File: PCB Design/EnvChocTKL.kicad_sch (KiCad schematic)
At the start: 188 parts

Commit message: added mid-mount type-c port, swapped onboard MCU for pico and also couple more mount holes, various other adjustments i.e backplate n stuff
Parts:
- removed USB1: TYPE-C-31-M-12, HRO-TYPE-C31-M-12:HRO-TYPE-C-31-M-12, symbol Type-C:HRO-TYPE-C-31-M-12
- added H5, H6: MountingHole_Pad, MountingHole:MountingHole_2.5mm_Pad, symbol Mechanical:MountingHole_Pad
- added J1: Type-c-31-m-14, josh-connectors:USB_C_TYPE-C-31-M-14, symbol josh-connector:USB_C_U262-161N-4BVC11
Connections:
- net GND: now also H5.1, H6.1, J1.A1 (GND), J1.A12 (GND), J1.B1 (GND), J1.B12 (GND), J1.S1 (SHIELD)
- net USB_D+: now also J1.A6 (D+), J1.B6 (D+)
- net USB_D-: now also J1.A7 (D-), J1.B7 (D-)
- net VBUS: now also RPI1.40 (VBUS), J1.A4 (VBUS), J1.A9 (VBUS), J1.B4 (VBUS), J1.B9 (VBUS)
- net at R6.2: now also J1.B5 (CC2)
- net at R5.2: now also J1.A5 (CC1)
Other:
- moved on the sheet: D_0, D_1, D_10, D_11, D_12, D_13, D_14, D_15, D_16, D_17, D_18, D_19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

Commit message: generated updated gerber
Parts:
- R5, R6: value 5.1K 0402 -> 5.1K 0805; footprint Resistor_SMD:R_0402_1005Metric -> Resistor_SMD:R_0805_2012Metric
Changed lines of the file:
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@@
   (symbol (lib_id "Device:R_Small") (at 50.165 46.355 270) (unit 1)
     (in_bom yes) (on_board yes)
-    (property "Reference" "R6" (id 0) (at 50.165 43.815 90))
-    (property "Value" "5.1K 0402" (id 1) (at 50.165 46.355 90)
+    (property "Reference" "R6" (id 0) (at 50.165 48.26 90))
+    (property "Value" "5.1K 0805" (id 1) (at 50.165 46.355 90)
       (effects (font (size 0.508 0.508)))
     )
-    (property "Footprint" "Resistor_SMD:R_0402_1005Metric" (id 2) (at 50.165 46.355 0)
+    (property "Footprint" "Resistor_SMD:R_0805_2012Metric" (id 2) (at 50.165 46.355 0)
       (effects (font (size 1.27 1.27)) hide)
     )
@@
     (in_bom yes) (on_board yes)
     (property "Reference" "R5" (id 0) (at 50.165 41.275 90))
-    (property "Value" "5.1K 0402" (id 1) (at 50.165 43.815 90)
+    (property "Value" "5.1K 0805" (id 1) (at 50.165 43.815 90)
       (effects (font (size 0.508 0.508)))
     )
-    (property "Footprint" "Resistor_SMD:R_0402_1005Metric" (id 2) (at 50.165 43.815 0)
+    (property "Footprint" "Resistor_SMD:R_0805_2012Metric" (id 2) (at 50.165 43.815 0)
       (effects (font (size 1.27 1.27)) hide)
     )
@@
     )
     (path "/00000000-0000-0000-0000-00006093a5b0"
-      (reference "R5") (unit 1) (value "5.1K 0402") (footprint "Resistor_SMD:R_0402_1005Metric")
+      (reference "R5") (unit 1) (value "5.1K 0805") (footprint "Resistor_SMD:R_0805_2012Metric")
     )
     (path "/00000000-0000-0000-0000-0000609385d4"
-      (reference "R6") (unit 1) (value "5.1K 0402") (footprint "Resistor_SMD:R_0402_1005Metric")
+      (reference "R6") (unit 1) (value "5.1K 0805") (footprint "Resistor_SMD:R_0805_2012Metric")
     )
     (path "/6be092fb-5a07-4210-ab9f-d96af1d79bdc"

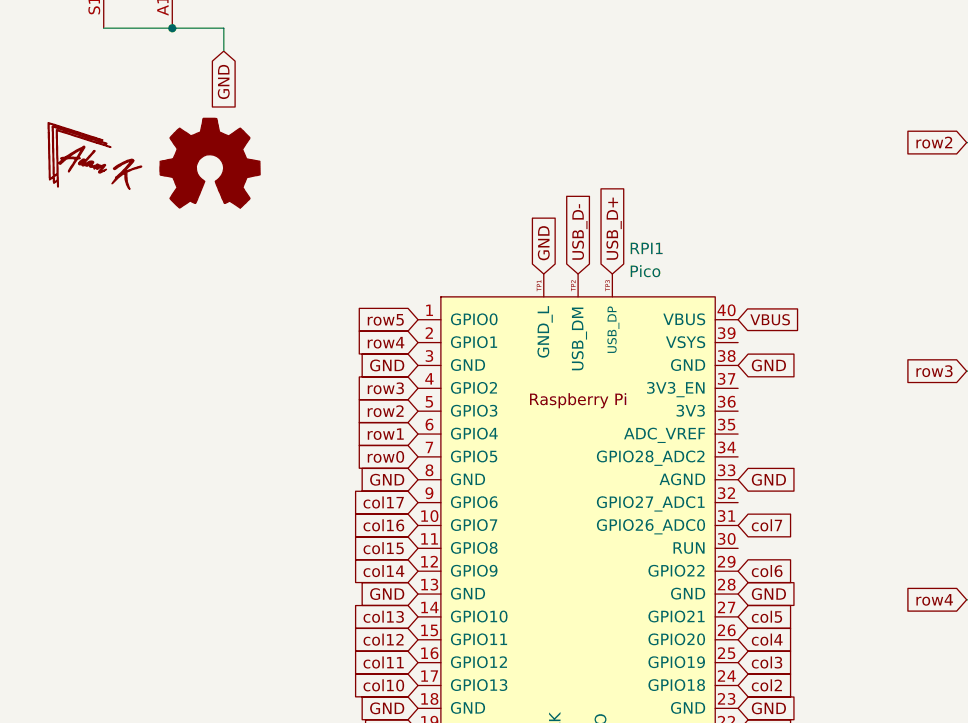
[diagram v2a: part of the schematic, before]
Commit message: modified footprint to have TP6 and added reset and bootsel buttons
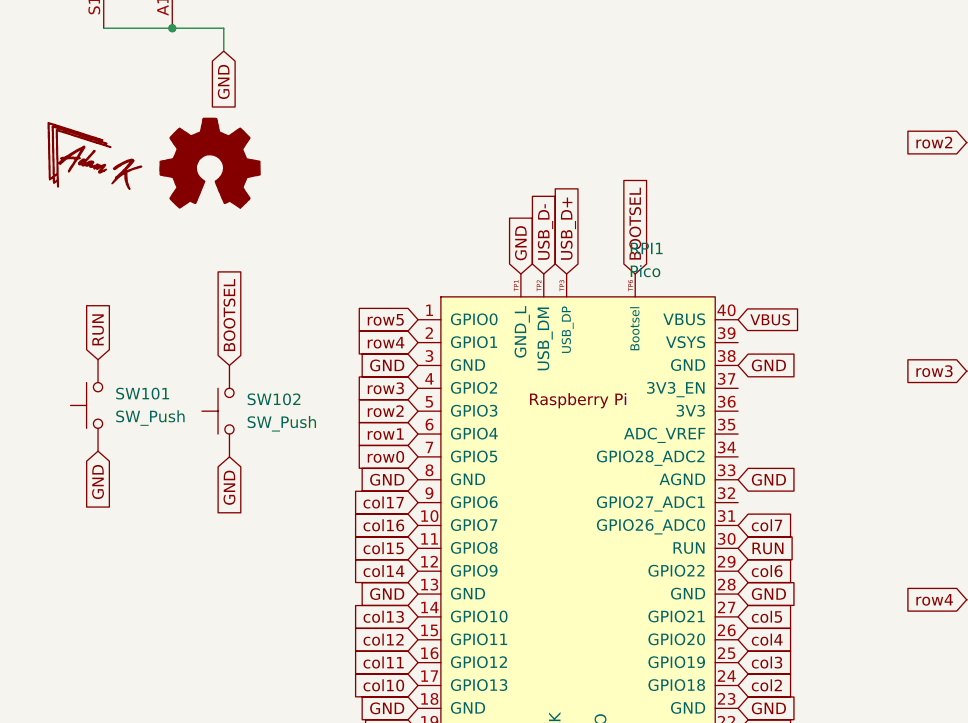
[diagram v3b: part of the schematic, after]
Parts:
- added SW101, SW102: SW_Push, Button_Switch_SMD:Panasonic_EVQPUJ_EVQPUA, symbol Switch:SW_Push
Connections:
- net GND: now also SW101.1, SW102.1
- net RUN: now reaches RPI1.30 (RUN)
- net RUN: now also SW101.2
- new net BOOTSEL: RPI1.TP6 (Bootsel), SW102.2
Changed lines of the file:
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@@
     (effects (font (size 1.27 1.27)) (justify left bottom))
   )
+  (global_label "BOOTSEL" (shape input) (at 38.735 114.3 90) (fields_autoplaced)
+    (effects (font (size 1.27 1.27)) (justify left))
+    (property "Intersheet References" "${INTERSHEET_REFS}" (id 0) (at 38.6556 103.6906 90)
+      (effects (font (size 1.27 1.27)) (justify left) hide)
+    )
+  )
   (global_label "col3" (shape input) (at 219.71 19.685 180) (fields_autoplaced)
     (effects (font (size 1.27 1.27)) (justify right))
@@
     )
   )
-  (global_label "GND" (shape input) (at 73.66 104.14 90) (fields_autoplaced)
+  (global_label "GND" (shape input) (at 71.12 104.14 90) (fields_autoplaced)
     (effects (font (size 1.27 1.27)) (justify left))
-    (property "Intersheet References" "${INTERSHEET_REFS}" (id 0) (at 12.7 132.08 0)
+    (property "Intersheet References" "${INTERSHEET_REFS}" (id 0) (at 10.16 132.08 0)
       (effects (font (size 1.27 1.27)) hide)
     )
   )
-  (global_label "USB_D+" (shape input) (at 81.28 104.14 90) (fields_autoplaced)
+  (global_label "USB_D+" (shape input) (at 76.2 104.14 90) (fields_autoplaced)
+    (effects (font (size 1.27 1.27)) (justify left))
+    (property "Intersheet References" "${INTERSHEET_REFS}" (id 0) (at 76.1206 94.1958 90)
+      (effects (font (size 1.27 1.27)) (justify left) hide)
+    )
+  )
+  (global_label "RUN" (shape input) (at 24.13 113.665 90) (fields_autoplaced)
     (effects (font (size 1.27 1.27)) (justify left))
-    (property "Intersheet References" "${INTERSHEET_REFS}" (id 0) (at 81.2006 94.1958 90)
+    (property "Intersheet References" "${INTERSHEET_REFS}" (id 0) (at 24.0506 107.4098 90)
       (effects (font (size 1.27 1.27)) (justify left) hide)
     )
   )
-  (global_label "USB_D-" (shape input) (at 77.47 104.14 90) (fields_autoplaced)
+  (global_label "USB_D-" (shape input) (at 73.66 104.14 90) (fields_autoplaced)
     (effects (font (size 1.27 1.27)) (justify left))
-    (property "Intersheet References" "${INTERSHEET_REFS}" (id 0) (at 77.3906 94.1958 90)
+    (property "Intersheet References" "${INTERSHEET_REFS}" (id 0) (at 73.5806 94.1958 90)
       (effects (font (size 1.27 1.27)) (justify left) hide)
     )
@@
     )
   )
+  (global_label "GND" (shape input) (at 24.13 123.825 270) (fields_autoplaced)
+    (effects (font (size 1.27 1.27)) (justify right))
+    (property "Intersheet References" "${INTERSHEET_REFS}" (id 0) (at 24.0506 130.0197 90)
+      (effects (font (size 1.27 1.27)) (justify right) hide)
+    )
+  )
   (global_label "row2" (shape input) (at 120.65 89.535 180) (fields_autoplaced)
     (effects (font (size 1.27 1.27)) (justify right))
@@
     )
   )
+  (global_label "RUN" (shape input) (at 95.25 134.62 0) (fields_autoplaced)
+    (effects (font (size 1.27 1.27)) (justify left))
+    (property "Intersheet References" "${INTERSHEET_REFS}" (id 0) (at 101.5052 134.5406 0)
+      (effects (font (size 1.27 1.27)) (justify left) hide)
+    )
+  )
   (global_label "col13" (shape input) (at 59.69 142.24 180) (fields_autoplaced)
     (effects (font (size 1.27 1.27)) (justify right))
@@
     )
   )
+  (global_label "BOOTSEL" (shape input) (at 83.82 104.14 90) (fields_autoplaced)
+    (effects (font (size 1.27 1.27)) (justify left))
+    (property "Intersheet References" "${INTERSHEET_REFS}" (id 0) (at 83.7406 93.5306 90)
+      (effects (font (size 1.27 1.27)) (justify left) hide)
+    )
+  )
   (global_label "col5" (shape input) (at 95.25 142.24 0) (fields_autoplaced)
     (effects (font (size 1.27 1.27)) (justify left))
@@
     )
   )
+  (global_label "GND" (shape input) (at 38.735 124.46 270) (fields_autoplaced)
+    (effects (font (size 1.27 1.27)) (justify right))
+    (property "Intersheet References" "${INTERSHEET_REFS}" (id 0) (at 38.6556 130.6547 90)
+      (effects (font (size 1.27 1.27)) (justify right) hide)
+    )
+  )
   (global_label "col7" (shape input) (at 95.25 132.08 0) (fields_autoplaced)
     (effects (font (size 1.27 1.27)) (justify left))
@@
     )
   )
+  (symbol (lib_id "Switch:SW_Push") (at 24.13 118.745 90) (unit 1)
+    (in_bom yes) (on_board yes) (fields_autoplaced)
+    (property "Reference" "SW101" (id 0) (at 26.035 117.4749 90)
+      (effects (font (size 1.27 1.27)) (justify right))
+    )
+    (property "Value" "SW_Push" (id 1) (at 26.035 120.0149 90)
+      (effects (font (size 1.27 1.27)) (justify right))
+    )
+    (property "Footprint" "Button_Switch_SMD:Panasonic_EVQPUJ_EVQPUA" (id 2) (at 19.05 118.745 0)
+      (effects (font (size 1.27 1.27)) hide)
+    )
+    (property "Datasheet" "~" (id 3) (at 19.05 118.745 0)
+      (effects (font (size 1.27 1.27)) hide)
+    )
+    (pin "1")
+    (pin "2")
+  )
   (symbol (lib_id "PicoModified:Pico") (at 77.47 133.35 0) (unit 1)
     (in_bom yes) (on_board yes) (fields_autoplaced)
@@
       (effects (font (size 1.27 1.27)) (justify left))
     )
-    (property "Footprint" "MCU_RaspberryPi_and_Boards:RPi_Pico_SMD_TH_MODIFIED" (id 2) (at 77.47 133.35 90)
+    (property "Footprint" "MCU_RaspberryPi_and_Boards:RPi_Pico_SMD_TH_MODIFIED" (id 2) (at 77.47 173.99 0)
       (effects (font (size 1.27 1.27)) hide)
     )
@@
     (pin "TP2")
     (pin "TP3")
+    (pin "TP6")
   )
   (symbol (lib_id "Mechanical:MountingHole_Pad") (at 52.07 174.625 0) (unit 1)
@@
     (pin "1")
   )
+  (symbol (lib_id "Switch:SW_Push") (at 38.735 119.38 90) (unit 1)
+    (in_bom yes) (on_board yes) (fields_autoplaced)
+    (property "Reference" "SW102" (id 0) (at 40.64 118.1099 90)
+      (effects (font (size 1.27 1.27)) (justify right))
+    )
+    (property "Value" "SW_Push" (id 1) (at 40.64 120.6499 90)
+      (effects (font (size 1.27 1.27)) (justify right))
+    )
+    (property "Footprint" "Button_Switch_SMD:Panasonic_EVQPUJ_EVQPUA" (id 2) (at 33.655 119.38 0)
+      (effects (font (size 1.27 1.27)) hide)
+    )
+    (property "Datasheet" "~" (id 3) (at 33.655 119.38 0)
+      (effects (font (size 1.27 1.27)) hide)
+    )
+    (pin "1")
+    (pin "2")
+  )
   (symbol (lib_id "josh-connector:USB_C_U262-161N-4BVC11") (at 32.385 53.975 0) (unit 1)
     (in_bom yes) (on_board yes) (fields_autoplaced)
@@
       (reference "RPI1") (unit 1) (value "Pico") (footprint "MCU_RaspberryPi_and_Boards:RPi_Pico_SMD_TH_MODIFIED")
     )
+    (path "/1557f765-4cb9-43a3-8748-a26a66c0aebc"
+      (reference "SW101") (unit 1) (value "SW_Push") (footprint "Button_Switch_SMD:Panasonic_EVQPUJ_EVQPUA")
+    )
+    (path "/d38e0140-d461-42fe-b6bb-07a3f8524c4a"
+      (reference "SW102") (unit 1) (value "SW_Push") (footprint "Button_Switch_SMD:Panasonic_EVQPUJ_EVQPUA")
+    )
     (path "/00000000-0000-0000-0000-000061464bfa"

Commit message: made backplate and switch plate as well as adjusted main pcb mount holes for standoffs
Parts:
- D_0, D_1, D_10, D_11, D_12, D_13, D_14, D_15, D_16, D_17, D_18, D_19, D_2, D_20, D_21, D_22, D_23, D_24, D_25, D_26, D_27, D_28, D_29, D_3, D_30, D_31, D_32, D_33, D_34, D_35, D_36, D_37, D_38, D_39, D_4, D_40, D_41, D_42, D_43, D_44, D_45, D_46, D_47, D_48, D_49, D_5, D_50, D_51, D_52, D_53, D_54, D_55, D_56, D_57, D_58, D_59, D_6, D_60, D_61, D_62, D_63, D_64, D_65, D_66, D_67, D_68, D_69, D_7, D_70, D_71, D_72, D_73, D_74, D_75, D_76, D_77, D_78, D_79, D_8, D_80, D_81, D_82, D_83, D_84, D_85, D_86, D_87, D_9: value D -> 1N4148W
- H1, H2, H3, H4, H5, H6: footprint MountingHole:MountingHole_2.5mm_Pad -> MountingHole:MountingHole_3.2mm_M3
- SW101, SW102: value SW_Push -> EVQPU; footprint Button_Switch_SMD:Panasonic_EVQPUJ_EVQPUA -> Button_Switch_SMD:Panasonic_EVQPUL_EVQPUC

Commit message: checks and preparation to order
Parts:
- added D1, D2: 0805 LED, LED_SMD:LED_0805_2012Metric, symbol Device:LED_Small
- added R1, R2: 0402 470r, Resistor_SMD:R_0402_1005Metric, symbol Device:R_Small
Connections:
- net GND: now also D1.1 (K), D2.1 (K)
- net at RPI1.32 (GPIO27_ADC1): now also R1.1
- net at RPI1.34 (GPIO28_ADC2): now also R2.1
- new net: D1.2 (A), R1.2
- new net: D2.2 (A), R2.2
